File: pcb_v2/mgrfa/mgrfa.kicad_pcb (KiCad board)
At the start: 2 copper layers, 127 x 66 mm, 20 parts, among them J1 sr8a_A, J10 designador, J2 sr8a_B, J3 sr8a_C, J4 sr8a_D, J5 sr8a_E, J6 sr8a_H, J7 sr8a_L, J8 bus_mgrf_1, J9 bus_mgrf_2, U1 74LS244, U2 74LS244

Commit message: projeto enviado para impressao em dezembro/25
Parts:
- D1: value LED -> POWER
- D2: value LED -> READ
- D3: value LED -> WRITE
- moved J9 15.9 mm to (128.3, 71.8)
- moved C1 15.9 mm to (153.0, 50.8)
- moved C2 15.9 mm to (126.4, 21.6)
- moved J1 15.9 mm to (36.8, 22.9)
- moved J10 15.9 mm to (41.3, 74.3)
- moved J2 15.9 mm to (50.2, 22.9)
- moved J3 15.9 mm to (62.9, 22.9)
- moved J4 15.9 mm to (75.6, 22.9)
- moved J5 15.9 mm to (88.3, 22.9)
- moved J6 15.9 mm to (101.0, 22.9)
- moved J7 15.9 mm to (113.7, 22.9)
- moved J8 15.9 mm to (151.8, 71.8)
- moved R1 15.9 mm to (126.4, 65.4)
- moved R2 15.9 mm to (136.5, 65.4)
- moved R3 15.9 mm to (146.7, 65.4)
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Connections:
- J8 pad 1: /data_7 -> +5V
- J8 pad 10: GND -> unconnected-(J8-Pin_10-Pad10)
- J8 pad 12: GND -> unconnected-(J8-Pin_12-Pad12)
- J8 pad 14: GND -> /data_0
- J8 pad 15: /data_0 -> GND
- J8 pad 4: +5V -> /data_7
- J8 pad 6: +5V -> unconnected-(J8-Pin_6-Pad6)
- J8 pad 8: +5V -> unconnected-(J8-Pin_8-Pad8)
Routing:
- net GND: track 95.3 -> 0.63 mm, vias 2 -> 9
- net n_read_B: track 45.0 -> 33.0 mm
- net n_read_A: track 45.7 -> 52.8 mm
- net /data_0: track 65.4 -> 69.8 mm
- net +5V: track 360.2 -> 364.6 mm
- net /data_7: track 66.2 -> 69.8 mm
- net /data_1: track 74.1 -> 75.9 mm
- net /data_6: track 61.8 -> 63.3 mm
- net /data_2: track 70.1 -> 71.3 mm
- net wr_addr_4: track 66.6 -> 67.7 mm
- net data_out_enable: track 100.2 -> 101.3 mm
- net clock: track 61.0 -> 62.1 mm
- net data_out_5: track 106.5 -> 105.5 mm
- net wr_addr_3: track 72.2 -> 73.2 mm
- net wr_addr_2: track 79.3 -> 80.1 mm
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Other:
- board size 127 x 66 mm -> 154.3 x 66 mm
- board text added: "Rev.A1 dezembro/2025"
- board text removed: "Rev.A1 julho/2025"

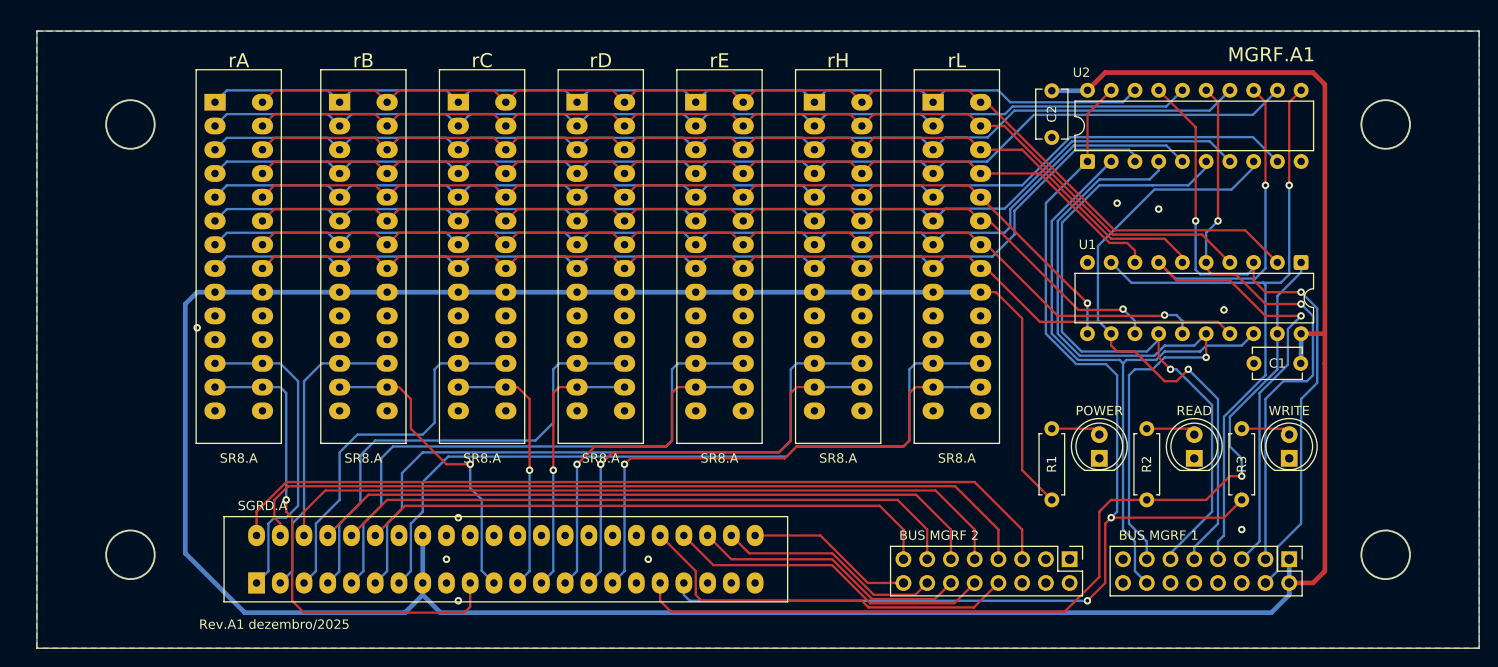
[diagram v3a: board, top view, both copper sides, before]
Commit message: revisao completa; mgrfa agora inclui sr8 e sgrda; remover estes dois no proximo commit
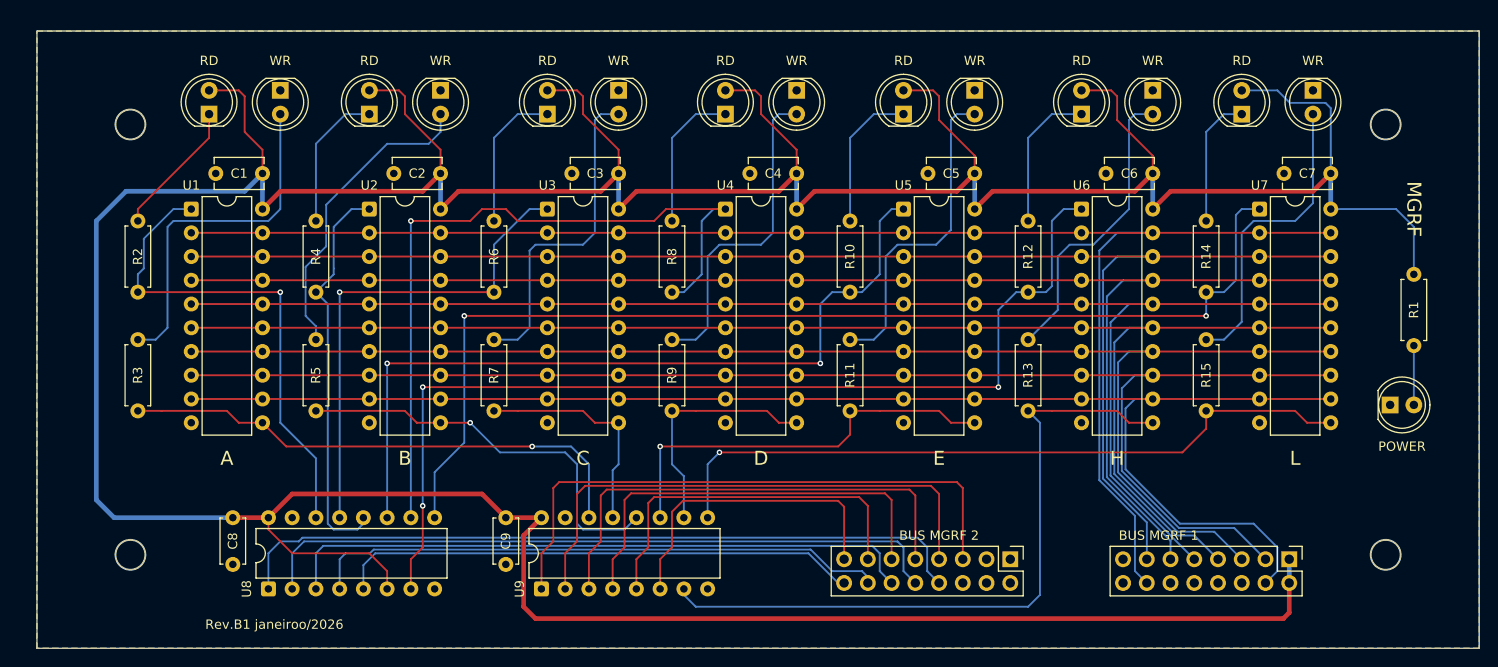
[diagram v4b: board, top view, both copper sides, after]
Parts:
- removed J1: sr8a_A, edge_connector:male-edge-connector-28
- removed J10: designador, edge_connector:male-edge-connector-44
- removed J2: sr8a_B, edge_connector:male-edge-connector-28
- removed J3: sr8a_C, edge_connector:male-edge-connector-28
- removed J4: sr8a_D, edge_connector:male-edge-connector-28
- removed J5: sr8a_E, edge_connector:male-edge-connector-28
- removed J6: sr8a_H, edge_connector:male-edge-connector-28
- removed J7: sr8a_L, edge_connector:male-edge-connector-28
- added C3: 100nF, Capacitor_THT:C_Disc_D5.1mm_W3.2mm_P5.00mm, F.Cu at (80.0, 30.5)
- added C4: 100nF, Capacitor_THT:C_Disc_D5.1mm_W3.2mm_P5.00mm, F.Cu at (99.1, 30.5)
- added C5: 100nF, Capacitor_THT:C_Disc_D5.1mm_W3.2mm_P5.00mm, F.Cu at (118.1, 30.5)
- added C6: 100nF, Capacitor_THT:C_Disc_D5.1mm_W3.2mm_P5.00mm, F.Cu at (137.2, 30.5)
- added C7: 100nF, Capacitor_THT:C_Disc_D5.1mm_W3.2mm_P5.00mm, F.Cu at (156.2, 30.5)
- added C8: 100nF, Capacitor_THT:C_Disc_D4.7mm_W2.5mm_P5.00mm, F.Cu at (38.7, 67.3)
- added C9: 100nF, Capacitor_THT:C_Disc_D4.7mm_W2.5mm_P5.00mm, F.Cu at (67.9, 67.3)
- added D10: RD, LED_THT:LED_D5.0mm, F.Cu at (110.5, 24.1)
- added D11: WR, LED_THT:LED_D5.0mm, F.Cu at (118.1, 21.6)
- added D12: RD, LED_THT:LED_D5.0mm, F.Cu at (129.5, 24.1)
- added D13: WR, LED_THT:LED_D5.0mm, F.Cu at (137.2, 21.6)
- added D14: RD, LED_THT:LED_D5.0mm, F.Cu at (146.7, 24.1)
- added D15: WR, LED_THT:LED_D5.0mm, F.Cu at (154.3, 21.6)
- added D4: RD, LED_THT:LED_D5.0mm, F.Cu at (53.3, 24.1)
- added D5: WR, LED_THT:LED_D5.0mm, F.Cu at (61.0, 21.6)
- added D6: RD, LED_THT:LED_D5.0mm, F.Cu at (72.4, 24.1)
- added D7: WR, LED_THT:LED_D5.0mm, F.Cu at (80.0, 21.6)
- added D8: RD, LED_THT:LED_D5.0mm, F.Cu at (91.4, 24.1)
- added D9: WR, LED_THT:LED_D5.0mm, F.Cu at (99.1, 21.6)
- added R10: 1K, Resistor_THT:R_Axial_DIN0207_L6.3mm_D2.5mm_P7.62mm_Horizontal, F.Cu at (104.8, 43.2)
- added R11: 1K, Resistor_THT:R_Axial_DIN0207_L6.3mm_D2.5mm_P7.62mm_Horizontal, F.Cu at (104.8, 55.9)
- added R12: 1K, Resistor_THT:R_Axial_DIN0207_L6.3mm_D2.5mm_P7.62mm_Horizontal, F.Cu at (123.8, 43.2)
- added R13: 1K, Resistor_THT:R_Axial_DIN0207_L6.3mm_D2.5mm_P7.62mm_Horizontal, F.Cu at (123.8, 55.9)
- added R14: 1K, Resistor_THT:R_Axial_DIN0207_L6.3mm_D2.5mm_P7.62mm_Horizontal, F.Cu at (142.9, 43.2)
- added R15: 1K, Resistor_THT:R_Axial_DIN0207_L6.3mm_D2.5mm_P7.62mm_Horizontal, F.Cu at (142.9, 55.9)
- added R4: 1K, Resistor_THT:R_Axial_DIN0207_L6.3mm_D2.5mm_P7.62mm_Horizontal, F.Cu at (47.6, 43.2)
- added R5: 1K, Resistor_THT:R_Axial_DIN0207_L6.3mm_D2.5mm_P7.62mm_Horizontal, F.Cu at (47.6, 55.9)
- added R6: 1K, Resistor_THT:R_Axial_DIN0207_L6.3mm_D2.5mm_P7.62mm_Horizontal, F.Cu at (66.7, 43.2)
- added R7: 1K, Resistor_THT:R_Axial_DIN0207_L6.3mm_D2.5mm_P7.62mm_Horizontal, F.Cu at (66.7, 55.9)
- added R8: 1K, Resistor_THT:R_Axial_DIN0207_L6.3mm_D2.5mm_P7.62mm_Horizontal, F.Cu at (85.7, 43.2)
- added R9: 1K, Resistor_THT:R_Axial_DIN0207_L6.3mm_D2.5mm_P7.62mm_Horizontal, F.Cu at (85.7, 55.9)
- added U3: 74LS574, Package_DIP:DIP-20_W7.62mm, F.Cu at (72.4, 34.3)
- added U4: 74LS574, Package_DIP:DIP-20_W7.62mm, F.Cu at (91.4, 34.3)
- added U5: 74LS574, Package_DIP:DIP-20_W7.62mm, F.Cu at (110.5, 34.3)
- added U6: 74LS574, Package_DIP:DIP-20_W7.62mm, F.Cu at (129.5, 34.3)
- added U7: 74LS574, Package_DIP:DIP-20_W7.62mm, F.Cu at (148.6, 34.3)
- added U8: 74LS138, Package_DIP:DIP-16_W7.62mm, F.Cu at (42.5, 74.9)
- added U9: 74HC238, Package_DIP:DIP-16_W7.62mm, F.Cu at (71.8, 74.9)
- D2: value READ -> RD
- D3: value WRITE -> WR
- U1, U2: value 74LS244 -> 74LS574
- moved U1 118.9 mm to (34.3, 34.3), turned to 0 degrees
- moved R3 118.5 mm to (28.6, 55.9)
- moved D3 114.9 mm to (43.8, 21.6), turned to -90 degrees
- moved C1 112.9 mm to (41.9, 30.5)
- moved D2 111.7 mm to (36.2, 24.1)
- moved R2 110.2 mm to (28.6, 43.2)
- moved U2 77.0 mm to (53.3, 34.3), turned to 0 degrees
- moved C2 66.0 mm to (61.0, 30.5), turned to 180 degrees
- moved R1 45.6 mm to (165.1, 41.3), turned to -90 degrees
- moved D1 31.6 mm to (162.6, 55.2), turned to 0 degrees
- moved J9 6.35 mm to (121.9, 71.8)
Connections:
- D2 pad 1: GND -> Net-(D2-K)
- D2 pad 2: Net-(D2-A) -> +5V
- J8 pad 11: /data_2 -> data_2
- J8 pad 13: /data_1 -> data_1
- J8 pad 14: /data_0 -> data_0
- J8 pad 3: /data_6 -> data_6
- J8 pad 4: /data_7 -> data_7
- J8 pad 5: /data_5 -> data_5
- J8 pad 7: /data_4 -> data_4
- J8 pad 9: /data_3 -> data_3
- R2 pad 1: data_out_enable -> ~{read_A}
- R2 pad 2: Net-(D2-A) -> Net-(D2-K)
- R3 pad 1: data_in_enable -> write_A
- U1 pad 1: data_out_enable -> ~{read_A}
- U1 pad 11: data_out_4 -> write_A
- U1 pad 12: /data_3 -> data_7
- U1 pad 13: data_out_5 -> data_6
- U1 pad 14: /data_2 -> data_5
- U1 pad 15: data_out_6 -> data_4
- U1 pad 16: /data_1 -> data_3
- U1 pad 17: data_out_7 -> data_2
- U1 pad 18: /data_0 -> data_1
- U1 pad 19: data_out_enable -> data_0
- U1 pad 2: data_out_0 -> data_0
- U1 pad 3: /data_7 -> data_1
- U1 pad 4: data_out_1 -> data_2
- U1 pad 5: /data_6 -> data_3
- U1 pad 6: data_out_2 -> data_4
- U1 pad 7: /data_5 -> data_5
- U1 pad 8: data_out_3 -> data_6
- U1 pad 9: /data_4 -> data_7
- U2 pad 1: data_in_enable -> ~{read_B}
- U2 pad 11: /data_4 -> write_B
- U2 pad 12: data_in_3 -> data_7
- U2 pad 13: /data_5 -> data_6
- U2 pad 14: data_in_2 -> data_5
- U2 pad 15: /data_6 -> data_4
- U2 pad 16: data_in_1 -> data_3
- U2 pad 17: /data_7 -> data_2
- U2 pad 18: data_in_0 -> data_1
- U2 pad 19: data_in_enable -> data_0
- U2 pad 2: /data_0 -> data_0
- U2 pad 3: data_in_7 -> data_1
- U2 pad 4: /data_1 -> data_2
- U2 pad 5: data_in_6 -> data_3
- U2 pad 6: /data_2 -> data_4
- U2 pad 7: data_in_5 -> data_5
- U2 pad 8: /data_3 -> data_6
- U2 pad 9: data_in_4 -> data_7
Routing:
- net data_0: track 0.00 -> 166.1 mm
- net data_1: track 0.00 -> 160.7 mm
- net data_2: track 0.00 -> 158.5 mm
- net data_3: track 0.00 -> 156.3 mm
- net data_7: track 0.00 -> 155.8 mm
- net data_4: track 0.00 -> 155.6 mm
- net data_5: track 0.00 -> 155.0 mm
- net data_6: track 0.00 -> 153.9 mm
- net data_in_4: track 123.7 -> 0.00 mm
- net data_in_3: track 123.7 -> 0.00 mm
- net data_in_enable: track 123.3 -> 0.00 mm, vias 2 -> 0
- net data_out_0: track 122.0 -> 0.00 mm
- net data_in_5: track 119.3 -> 0.00 mm
- net ~{read_L}: track 0.00 -> 118.3 mm, vias 0 -> 2
- net data_in_2: track 117.5 -> 0.00 mm
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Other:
- outline, holes or cut-outs redrawn
- board text added: "A"
- board text added: "B"
- board text added: "C"
- board text added: "D"
- board text added: "E"
- board text added: "H"
- board text added: "L"
- board text added: "MGRF"
- board text added: "Rev.B1 janeiroo/2026"
- board text removed: "MGRF.A1"
- board text removed: "Rev.A1 dezembro/2025"
- board text removed: "SGRD.A"
- board text removed: "SR8.A"
- board text removed: "rA"
- board text removed: "rB"
- board text removed: "rC"
- board text removed: "rD"
- board text removed: "rE"
- board text removed: "rH"
- board text removed: "rL"

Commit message: concluida a revisão
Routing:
- net +5V: track 481.8 -> 452.2 mm
- net wr_addr_0: track 63.3 -> 50.3 mm
- net wr_addr_1: track 57.1 -> 44.9 mm
- net wr_addr_2: track 51.5 -> 39.4 mm
- net wr_addr_3: track 45.6 -> 34.0 mm
- net clock: track 33.6 -> 22.1 mm
- net wr_addr_4: track 39.6 -> 29.0 mm
- net write_H: track 73.9 -> 67.2 mm
- net Net-(D3-A): track 37.5 -> 34.9 mm
- net ~{read_C}: track 53.0 -> 54.1 mm
- net write_E: track 44.9 -> 45.5 mm, vias 1 -> 0
- net GND: vias 0 -> 2

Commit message: Update mgrfa.kicad_pcb and mgrfa.kicad_sch
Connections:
- net clock renamed write_clock
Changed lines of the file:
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@@
 	(net 36 "wr_addr_1")
 	(net 37 "wr_addr_2")
-	(net 38 "clock")
+	(net 38 "write_clock")
 	(net 39 "Net-(D1-A)")
 	(net 40 "Net-(D4-K)")
@@
 			(layers "*.Cu" "*.Mask")
 			(remove_unused_layers no)
-			(net 38 "clock")
+			(net 38 "write_clock")
 			(pinfunction "Pin_15")
 			(pintype "passive")
@@
 			(layers "*.Cu" "*.Mask")
 			(remove_unused_layers no)
-			(net 38 "clock")
+			(net 38 "write_clock")
 			(pinfunction "E3")
 			(pintype "input")

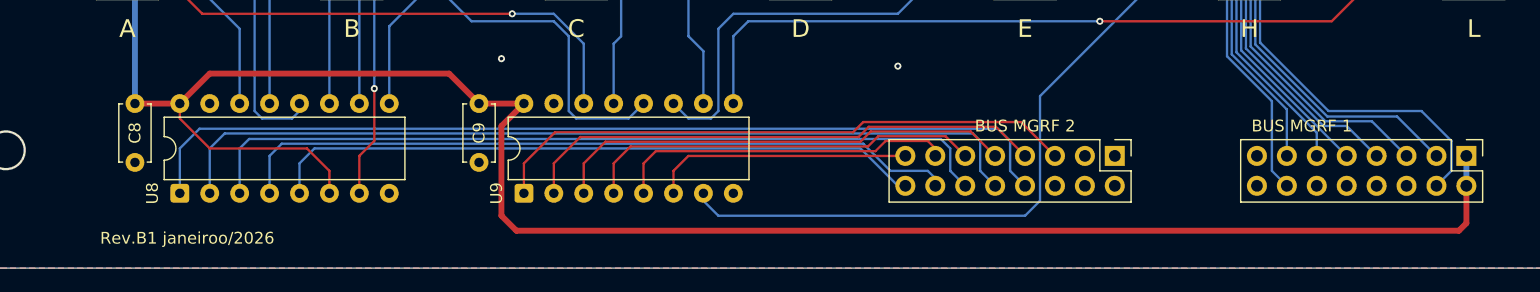
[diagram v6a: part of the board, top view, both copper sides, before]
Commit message: ajustes para envio para produção
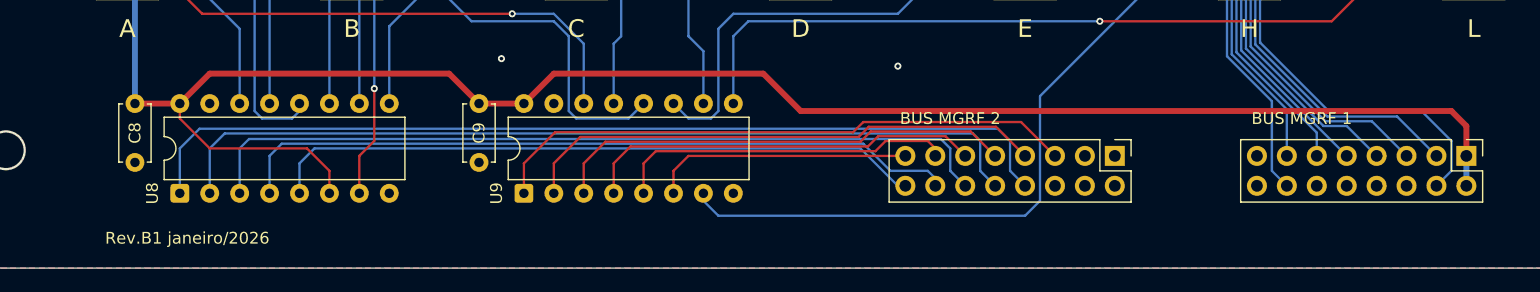
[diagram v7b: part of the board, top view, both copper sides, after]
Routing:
- net +5V: track 452.2 -> 441.4 mm
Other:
- board text added: "Rev.B1 janeiro/2026"
- board text removed: "Rev.B1 janeiroo/2026"
